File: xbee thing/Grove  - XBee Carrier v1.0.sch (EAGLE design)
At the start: 38 parts, among them J1 SULLINS_NPPN101BFCN-RCSULLINS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, J2 HEADER-10P_STANDARD, J3 HEADER-10P_STANDARD, J4 SULLINS_NPPN101BFCN-RCSULLINS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, Q4 FQ7050B-6.000, U1 TUSB2046BVF, U2 RT9167A_33PB, U4 FT232RL

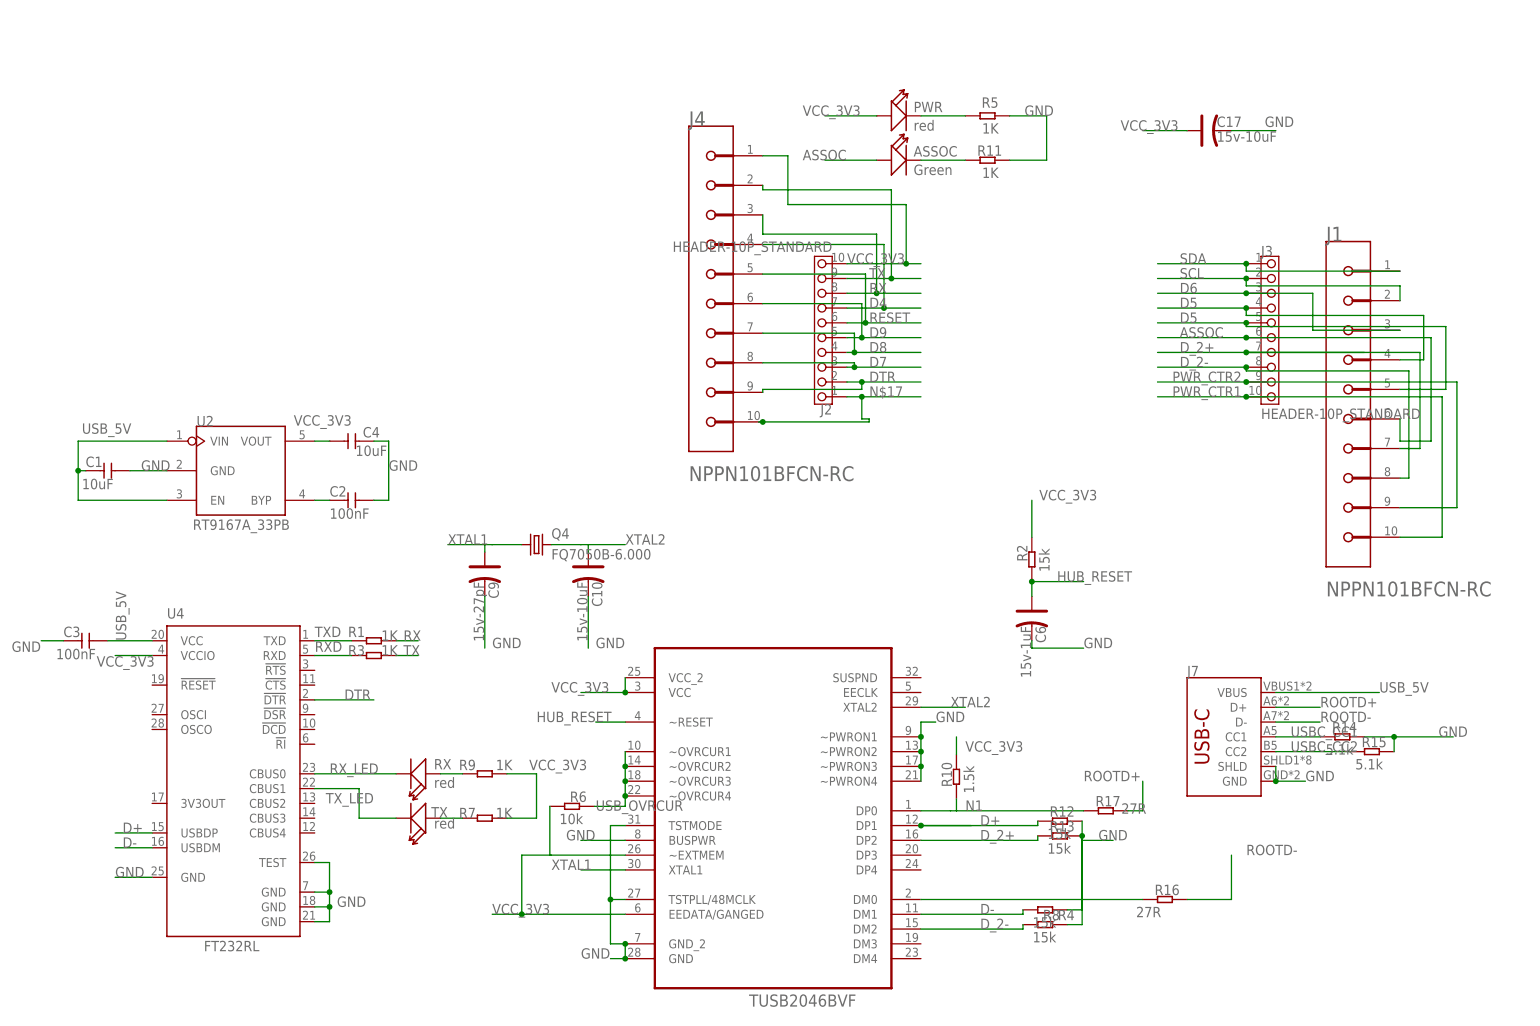
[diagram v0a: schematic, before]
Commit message: make the ground plane actually a plane and not airwires
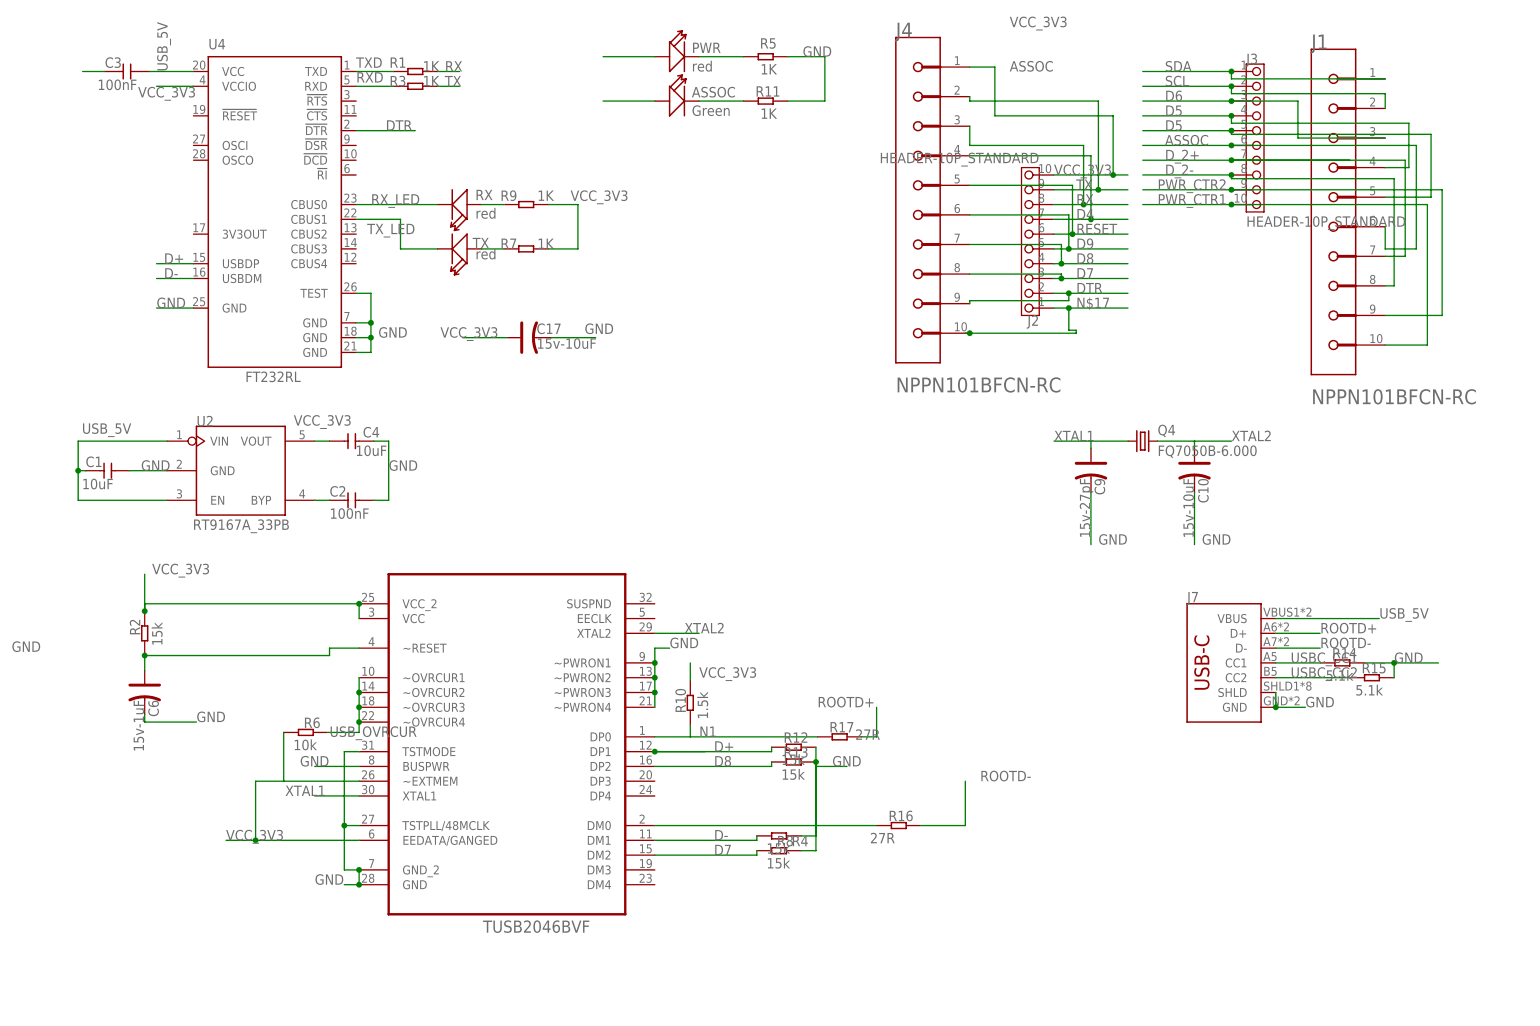
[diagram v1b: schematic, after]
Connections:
- net D7: now also R8.2, U1.DM2
- net D8: now also R13.2, U1.DP2
- net D_2+: no longer R13.2, U1.DP2
- net D_2-: no longer R8.2, U1.DM2
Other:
- moved on the sheet: ASSOC, C10, C17, C3, C6, C9, J1, J2, J3, J4, J7, PWR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
